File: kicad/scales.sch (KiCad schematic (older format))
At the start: 14 parts, among them J1 Serial, SW1 SW_DIP_x01, SW2 SW_DIP_x01, U1 AP2112

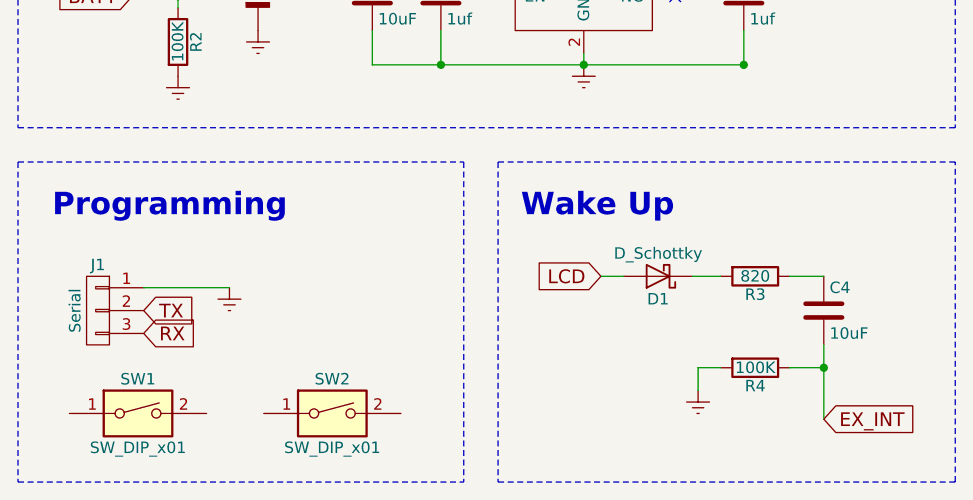
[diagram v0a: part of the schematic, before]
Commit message: Wake up is simply rising edge
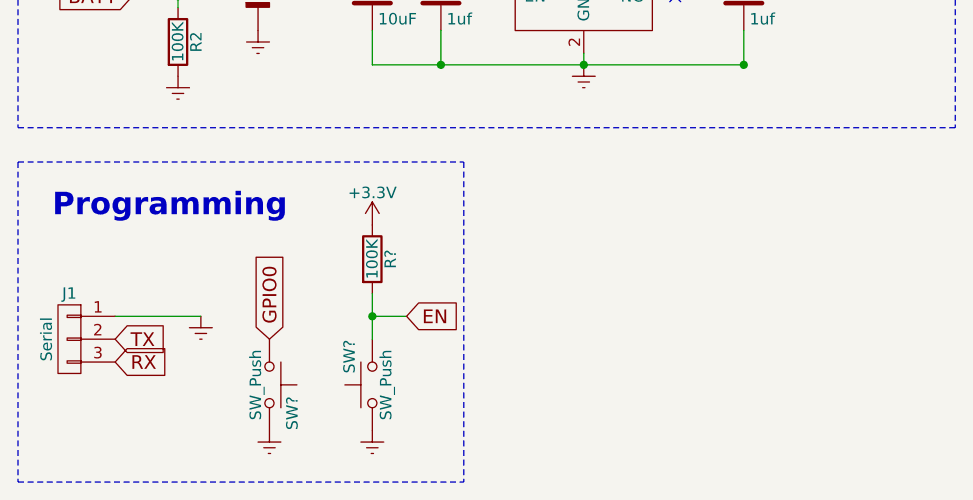
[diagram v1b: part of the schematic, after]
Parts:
- removed C4: 10uF, Capacitors_SMD:C_0805_HandSoldering, symbol C
- removed D1: D_Schottky, symbol D_Schottky
- removed R3: 820, Resistors_SMD:R_0805_HandSoldering, symbol R
- removed R4: 100K, Resistors_SMD:R_0805_HandSoldering, symbol R
- removed SW1, SW2: SW_DIP_x01, symbol SW_DIP_x01
- added R?: 100K, Resistors_SMD:R_0805_HandSoldering, symbol R
- added SW? (x2): SW_Push, symbol SW_Push
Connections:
- net +3V3: now also R?.1
- net Earth: now also SW?.1, SW?.2
- new net EN: R?.2, SW?.2
- new net GPIO0: SW?.1
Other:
- note removed: "Wake Up"
- moved on the sheet: J1
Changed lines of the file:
@@
 L Earth #PWR5
 U 1 1 59D62590
-P 1900 2825
-F 0 "#PWR5" H 1900 2575 50  0001 C CNN
-F 1 "Earth" H 1900 2675 50  0001 C CNN
-F 2 "" H 1900 2825 50  0000 C CNN
-F 3 "" H 1900 2825 50  0000 C CNN
-	1    1900 2825
-	-1   0    0    -1
-$EndComp
-$Comp
-L R R3
-U 1 1 59D62599
-P 4200 2775
-F 0 "R3" V 4280 2775 50  0000 C CNN
-F 1 "820" V 4200 2775 50  0000 C CNN
-F 2 "Resistors_SMD:R_0805_HandSoldering" V 4130 2775 50  0001 C CNN
-F 3 "" H 4200 2775 50  0000 C CNN
-	1    4200 2775
-	0    1    1    0
-$EndComp
-$Comp
-L Earth #PWR6
-U 1 1 59D6259A
-P 3950 3275
-F 0 "#PWR6" H 3950 3025 50  0001 C CNN
-F 1 "Earth" H 3950 3125 50  0001 C CNN
-F 2 "" H 3950 3275 50  0000 C CNN
-F 3 "" H 3950 3275 50  0000 C CNN
-	1    3950 3275
+P 1775 2950
+F 0 "#PWR5" H 1775 2700 50  0001 C CNN
+F 1 "Earth" H 1775 2800 50  0001 C CNN
+F 2 "" H 1775 2950 50  0000 C CNN
+F 3 "" H 1775 2950 50  0000 C CNN
+	1    1775 2950
 	-1   0    0    -1
 $EndComp
@@
 	1    0    0    -1
 $EndComp
-Text Notes 3175 2525 0    98   ~ 20
-Wake Up
 $Comp
 L Battery BT1
@@
 	1    0    0    -1
 $EndComp
-Text GLabel 1525 2925 2    60   Input ~ 0
+Text GLabel 1400 3050 2    60   Input ~ 0
 TX
-Text GLabel 1525 3025 2    60   Input ~ 0
+Text GLabel 1400 3150 2    60   Input ~ 0
 RX
 Text GLabel 1475 1550 0    60   Input ~ 0
@@
 Wire Wire Line
 	2825 1200 2825 1400
-Wire Notes Line
-	3075 2275 3075 3675
-Wire Notes Line
-	3075 3675 5075 3675
-Wire Notes Line
-	5075 3675 5075 2275
-Wire Notes Line
-	5075 2275 3075 2275
 Wire Notes Line
 	975  725  975  2125
@@
 	5075 725  5075 2125
 $Comp
-L C C4
-U 1 1 59D6390C
-P 4500 2925
-F 0 "C4" H 4525 3025 50  0000 L CNN
-F 1 "10uF" H 4525 2825 50  0000 L CNN
-F 2 "Capacitors_SMD:C_0805_HandSoldering" H 4538 2775 50  0001 C CNN
-F 3 "" H 4500 2925 50  0000 C CNN
-	1    4500 2925
-	1    0    0    -1
-$EndComp
-Text GLabel 3525 2775 0    60   Input ~ 0
-LCD
-$Comp
-L D_Schottky D1
-U 1 1 59D63AE4
-P 3775 2775
-F 0 "D1" H 3775 2875 50  0000 C CNN
-F 1 "D_Schottky" H 3775 2675 50  0000 C CNN
-F 2 "" H 3775 2775 50  0001 C CNN
-F 3 "" H 3775 2775 50  0001 C CNN
-	1    3775 2775
-	-1   0    0    1
-$EndComp
-Text GLabel 4500 3400 2    60   Input ~ 0
-EX_INT
-$Comp
-L R R4
-U 1 1 59D63D1D
-P 4200 3175
-F 0 "R4" V 4280 3175 50  0000 C CNN
-F 1 "100K" V 4200 3175 50  0000 C CNN
-F 2 "Resistors_SMD:R_0805_HandSoldering" V 4130 3175 50  0001 C CNN
-F 3 "" H 4200 3175 50  0000 C CNN
-	1    4200 3175
-	0    1    1    0
-$EndComp
-Wire Wire Line
-	3925 2775 4050 2775
-Wire Wire Line
-	3525 2775 3625 2775
-Wire Wire Line
-	4500 3075 4500 3400
-Wire Wire Line
-	4050 3175 3950 3175
-Wire Wire Line
-	3950 3175 3950 3275
-Wire Wire Line
-	4500 2775 4350 2775
-Wire Wire Line
-	4350 3175 4500 3175
-Connection ~ 4500 3175
-$Comp
 L CONN_01X03 J1
 U 1 1 59D64697
-P 1325 2925
-F 0 "J1" H 1325 3125 50  0000 C CNN
-F 1 "Serial" V 1425 2925 50  0000 C CNN
-F 2 "" H 1325 2925 50  0001 C CNN
-F 3 "" H 1325 2925 50  0001 C CNN
-	1    1325 2925
-	-1   0    0    -1
-$EndComp
-Wire Wire Line
-	1525 2825 1900 2825
-$Comp
-L SW_DIP_x01 SW1
-U 1 1 59D62C52
-P 1500 3375
-F 0 "SW1" H 1500 3525 50  0000 C CNN
-F 1 "SW_DIP_x01" H 1500 3225 50  0000 C CNN
-F 2 "" H 1500 3375 50  0001 C CNN
-F 3 "" H 1500 3375 50  0001 C CNN
-	1    1500 3375
-	1    0    0    -1
-$EndComp
-$Comp
-L SW_DIP_x01 SW2
-U 1 1 59D62D60
-P 2350 3375
-F 0 "SW2" H 2350 3525 50  0000 C CNN
-F 1 "SW_DIP_x01" H 2350 3225 50  0000 C CNN
-F 2 "" H 2350 3375 50  0001 C CNN
-F 3 "" H 2350 3375 50  0001 C CNN
-	1    2350 3375
-	1    0    0    -1
-$EndComp
+P 1200 3050
+F 0 "J1" H 1200 3250 50  0000 C CNN
+F 1 "Serial" V 1300 3050 50  0000 C CNN
+F 2 "" H 1200 3050 50  0001 C CNN
+F 3 "" H 1200 3050 50  0001 C CNN
+	1    1200 3050
+	-1   0    0    -1
+$EndComp
+Wire Wire Line
+	1400 2950 1775 2950
+$Comp
+L SW_Push SW?
+U 1 1 59D68B06
+P 2075 3250
+F 0 "SW?" H 2125 3350 50  0000 L CNN
+F 1 "SW_Push" H 2075 3190 50  0000 C CNN
+F 2 "" H 2075 3450 50  0001 C CNN
+F 3 "" H 2075 3450 50  0001 C CNN
+	1    2075 3250
+	0    1    1    0
+$EndComp
+$Comp
+L SW_Push SW?
+U 1 1 59D68B53
+P 2525 3250
+F 0 "SW?" H 2575 3350 50  0000 L CNN
+F 1 "SW_Push" H 2525 3190 50  0000 C CNN
+F 2 "" H 2525 3450 50  0001 C CNN
+F 3 "" H 2525 3450 50  0001 C CNN
+	1    2525 3250
+	0    -1   -1   0
+$EndComp
+Text GLabel 2075 3050 1    60   Input ~ 0
+GPIO0
+$Comp
+L Earth #PWR?
+U 1 1 59D68C6B
+P 2075 3450
+F 0 "#PWR?" H 2075 3200 50  0001 C CNN
+F 1 "Earth" H 2075 3300 50  0001 C CNN
+F 2 "" H 2075 3450 50  0000 C CNN
+F 3 "" H 2075 3450 50  0000 C CNN
+	1    2075 3450
+	-1   0    0    -1
+$EndComp
+Text GLabel 2675 2950 2    60   Input ~ 0
+EN
+$Comp
+L Earth #PWR?
+U 1 1 59D68D23
+P 2525 3450
+F 0 "#PWR?" H 2525 3200 50  0001 C CNN
+F 1 "Earth" H 2525 3300 50  0001 C CNN
+F 2 "" H 2525 3450 50  0000 C CNN
+F 3 "" H 2525 3450 50  0000 C CNN
+	1    2525 3450
+	-1   0    0    -1
+$EndComp
+$Comp
+L +3.3V #PWR?
+U 1 1 59D68DA9
+P 2525 2550
+F 0 "#PWR?" H 2525 2400 50  0001 C CNN
+F 1 "+3.3V" H 2525 2690 50  0000 C CNN
+F 2 "" H 2525 2550 50  0001 C CNN
+F 3 "" H 2525 2550 50  0001 C CNN
+	1    2525 2550
+	1    0    0    -1
+$EndComp
+$Comp
+L R R?
+U 1 1 59D68E04
+P 2525 2700
+F 0 "R?" V 2605 2700 50  0000 C CNN
+F 1 "100K" V 2525 2700 50  0000 C CNN
+F 2 "Resistors_SMD:R_0805_HandSoldering" V 2455 2700 50  0001 C CNN
+F 3 "" H 2525 2700 50  0001 C CNN
+	1    2525 2700
+	1    0    0    -1
+$EndComp
+Wire Wire Line
+	2525 2850 2525 3050
+Wire Wire Line
+	2675 2950 2525 2950
+Connection ~ 2525 2950
 $EndSCHEMATC

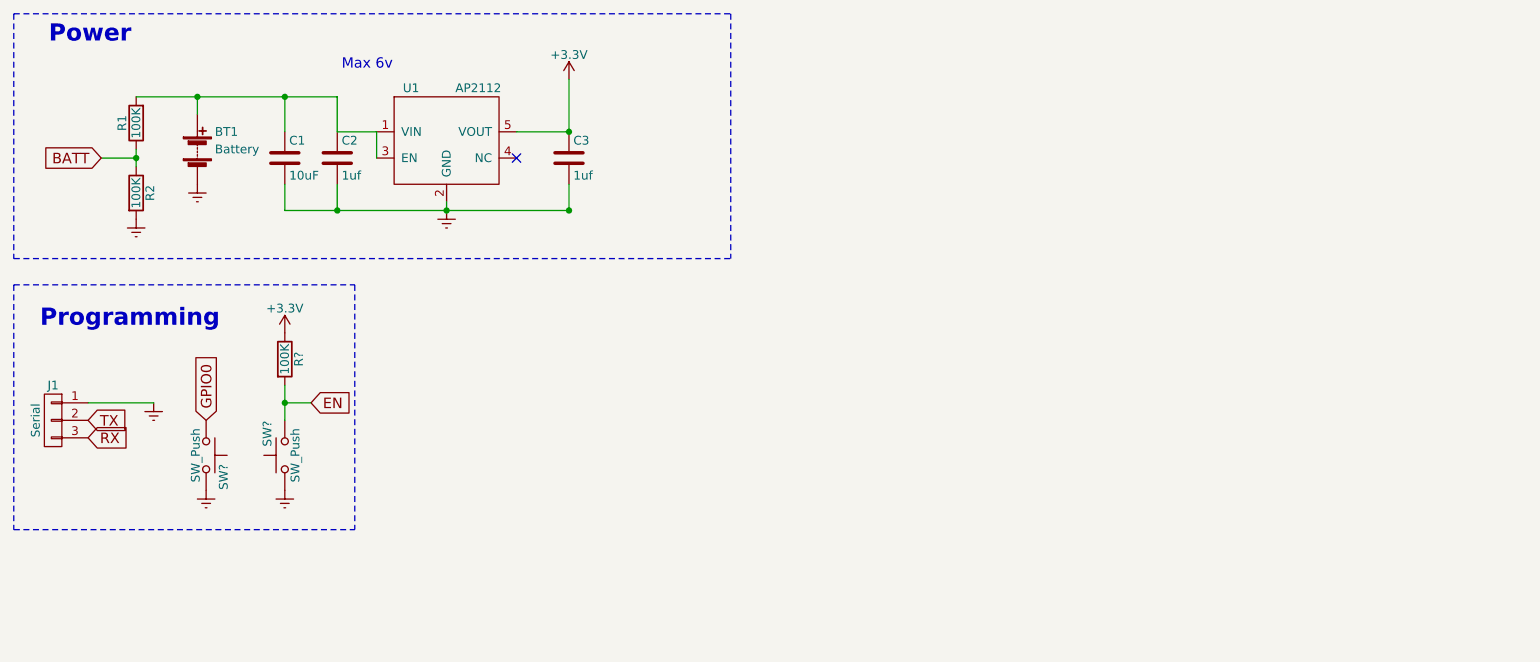
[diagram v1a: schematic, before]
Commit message: ESP32 WROOM
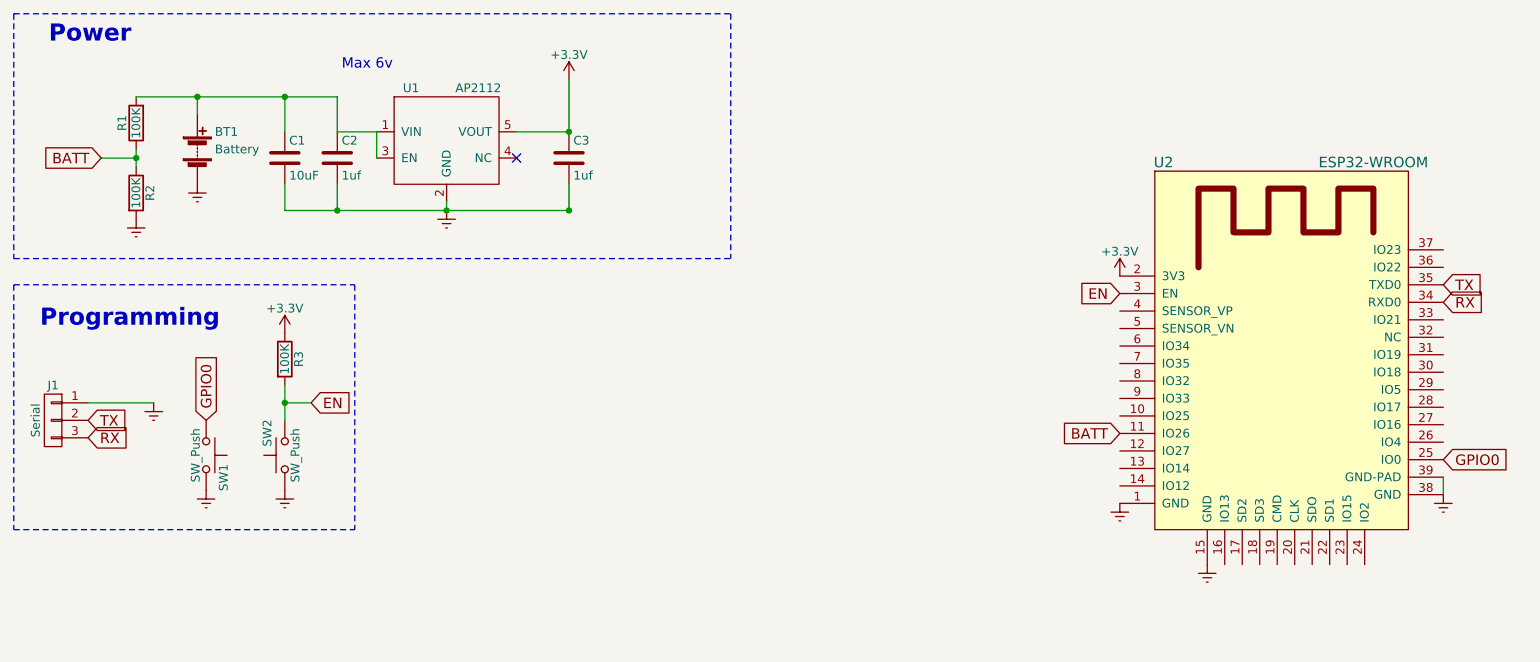
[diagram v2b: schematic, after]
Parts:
- added U2: ESP32-WROOM, ESP32-footprints-Lib:ESP32-WROOM, symbol ESP32-WROOM
- gave numbers to parts that had none: 3
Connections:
- net +3V3: now also U2.2 (3V3)
- net BATT: now also U2.11 (IO26)
- net EN: now also U2.3 (EN)
- net Earth: now also U2.1 (GND), U2.15 (GND), U2.38 (GND), U2.39 (GND-PAD)
- net GPIO0: now also U2.25 (IO0)
- net RX: now also U2.34 (RXD0)
- net TX: now also U2.35 (TXD0)
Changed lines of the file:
@@
 LIBS:valves
 LIBS:switches
+LIBS:ESP32-footprints-Shem-Lib
 LIBS:scales-cache
 EELAYER 25 0
@@
 $EndDescr
 $Comp
-L Earth #PWR5
+L Earth #PWR7
 U 1 1 59D62590
 P 1775 2950
-F 0 "#PWR5" H 1775 2700 50  0001 C CNN
+F 0 "#PWR7" H 1775 2700 50  0001 C CNN
 F 1 "Earth" H 1775 2800 50  0001 C CNN
 F 2 "" H 1775 2950 50  0000 C CNN
@@
 	1400 2950 1775 2950
 $Comp
-L SW_Push SW?
+L SW_Push SW1
 U 1 1 59D68B06
 P 2075 3250
-F 0 "SW?" H 2125 3350 50  0000 L CNN
+F 0 "SW1" H 2125 3350 50  0000 L CNN
 F 1 "SW_Push" H 2075 3190 50  0000 C CNN
 F 2 "" H 2075 3450 50  0001 C CNN
@@
 $EndComp
 $Comp
-L SW_Push SW?
+L SW_Push SW2
 U 1 1 59D68B53
 P 2525 3250
-F 0 "SW?" H 2575 3350 50  0000 L CNN
+F 0 "SW2" H 2575 3350 50  0000 L CNN
 F 1 "SW_Push" H 2525 3190 50  0000 C CNN
 F 2 "" H 2525 3450 50  0001 C CNN
@@
 GPIO0
 $Comp
-L Earth #PWR?
+L Earth #PWR8
 U 1 1 59D68C6B
 P 2075 3450
-F 0 "#PWR?" H 2075 3200 50  0001 C CNN
+F 0 "#PWR8" H 2075 3200 50  0001 C CNN
 F 1 "Earth" H 2075 3300 50  0001 C CNN
 F 2 "" H 2075 3450 50  0000 C CNN
@@
 EN
 $Comp
-L Earth #PWR?
+L Earth #PWR9
 U 1 1 59D68D23
 P 2525 3450
-F 0 "#PWR?" H 2525 3200 50  0001 C CNN
+F 0 "#PWR9" H 2525 3200 50  0001 C CNN
 F 1 "Earth" H 2525 3300 50  0001 C CNN
 F 2 "" H 2525 3450 50  0000 C CNN
@@
 $EndComp
 $Comp
-L +3.3V #PWR?
+L +3.3V #PWR6
 U 1 1 59D68DA9
 P 2525 2550
-F 0 "#PWR?" H 2525 2400 50  0001 C CNN
+F 0 "#PWR6" H 2525 2400 50  0001 C CNN
 F 1 "+3.3V" H 2525 2690 50  0000 C CNN
 F 2 "" H 2525 2550 50  0001 C CNN
@@
 $EndComp
 $Comp
-L R R?
+L R R3
 U 1 1 59D68E04
 P 2525 2700
-F 0 "R?" V 2605 2700 50  0000 C CNN
+F 0 "R3" V 2605 2700 50  0000 C CNN
 F 1 "100K" V 2525 2700 50  0000 C CNN
 F 2 "Resistors_SMD:R_0805_HandSoldering" V 2455 2700 50  0001 C CNN
@@
 	2675 2950 2525 2950
 Connection ~ 2525 2950
+$Comp
+L ESP32-WROOM U2
+U 1 1 59D7564C
+P 8250 2825
+F 0 "U2" H 7550 4075 60  0000 C CNN
+F 1 "ESP32-WROOM" H 8750 4075 60  0000 C CNN
+F 2 "ESP32-footprints-Lib:ESP32-WROOM" H 8600 4175 60  0001 C CNN
+F 3 "" H 7800 3275 60  0001 C CNN
+	1    8250 2825
+	1    0    0    -1
+$EndComp
+$Comp
+L +3.3V #PWR5
+U 1 1 59D75853
+P 7300 2225
+F 0 "#PWR5" H 7300 2075 50  0001 C CNN
+F 1 "+3.3V" H 7300 2365 50  0000 C CNN
+F 2 "" H 7300 2225 50  0001 C CNN
+F 3 "" H 7300 2225 50  0001 C CNN
+	1    7300 2225
+	1    0    0    -1
+$EndComp
+Text GLabel 7300 2325 0    60   Input ~ 0
+EN
+Text GLabel 9150 3275 2    60   Input ~ 0
+GPIO0
+Text GLabel 9150 2275 2    60   Input ~ 0
+TX
+Text GLabel 9150 2375 2    60   Input ~ 0
+RX
+$Comp
+L Earth #PWR12
+U 1 1 59D75FA7
+P 7800 3875
+F 0 "#PWR12" H 7800 3625 50  0001 C CNN
+F 1 "Earth" H 7800 3725 50  0001 C CNN
+F 2 "" H 7800 3875 50  0000 C CNN
+F 3 "" H 7800 3875 50  0000 C CNN
+	1    7800 3875
+	-1   0    0    -1
+$EndComp
+$Comp
+L Earth #PWR11
+U 1 1 59D76006
+P 7300 3525
+F 0 "#PWR11" H 7300 3275 50  0001 C CNN
+F 1 "Earth" H 7300 3375 50  0001 C CNN
+F 2 "" H 7300 3525 50  0000 C CNN
+F 3 "" H 7300 3525 50  0000 C CNN
+	1    7300 3525
+	-1   0    0    -1
+$EndComp
+$Comp
+L Earth #PWR10
+U 1 1 59D76035
+P 9150 3475
+F 0 "#PWR10" H 9150 3225 50  0001 C CNN
+F 1 "Earth" H 9150 3325 50  0001 C CNN
+F 2 "" H 9150 3475 50  0000 C CNN
+F 3 "" H 9150 3475 50  0000 C CNN
+	1    9150 3475
+	-1   0    0    -1
+$EndComp
+Wire Wire Line
+	9150 3375 9150 3475
+Text GLabel 7300 3125 0    60   Input ~ 0
+BATT
 $EndSCHEMATC

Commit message: Schematic
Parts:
- added J2: HX711, symbol CONN_01X04
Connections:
- net Earth: now also J2.4 (P4)
- net WCLK: now reaches U2.20 (CLK)
- net WCLK: now also J2.3 (P3)
- net WDATA: now reaches U2.21 (SDO)
- net WDATA: now also J2.2 (P2)
- net WAKE: now reaches U2.7 (IO35)
- net WAKE: now also J2.1 (P1)
- no-connect marks 1 -> 26
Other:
- note added: "HX711"
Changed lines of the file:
@@
 $EndDescr
 $Comp
-L Earth #PWR7
+L Earth #PWR8
 U 1 1 59D62590
 P 1775 2950
-F 0 "#PWR7" H 1775 2700 50  0001 C CNN
+F 0 "#PWR8" H 1775 2700 50  0001 C CNN
 F 1 "Earth" H 1775 2800 50  0001 C CNN
 F 2 "" H 1775 2950 50  0000 C CNN
@@
 	3450 1850 3450 1800
 Wire Wire Line
-	2525 1850 4150 1850
+	2525 1850 2825 1850
+Wire Wire Line
+	2825 1850 3450 1850
+Wire Wire Line
+	3450 1850 4150 1850
 Wire Wire Line
 	2825 1850 2825 1700
@@
 	3050 1550 3050 1400
 Wire Wire Line
-	1675 1200 2825 1200
+	1675 1200 2025 1200
+Wire Wire Line
+	2025 1200 2525 1200
+Wire Wire Line
+	2525 1200 2825 1200
 Wire Wire Line
 	2825 1200 2825 1400
@@
 Connection ~ 4150 1400
 Wire Wire Line
-	1675 1500 1675 1600
+	1675 1500 1675 1550
+Wire Wire Line
+	1675 1550 1675 1600
 Wire Wire Line
 	1675 1550 1475 1550
@@
 GPIO0
 $Comp
-L Earth #PWR8
+L Earth #PWR9
 U 1 1 59D68C6B
 P 2075 3450
-F 0 "#PWR8" H 2075 3200 50  0001 C CNN
+F 0 "#PWR9" H 2075 3200 50  0001 C CNN
 F 1 "Earth" H 2075 3300 50  0001 C CNN
 F 2 "" H 2075 3450 50  0000 C CNN
@@
 EN
 $Comp
-L Earth #PWR9
+L Earth #PWR10
 U 1 1 59D68D23
 P 2525 3450
-F 0 "#PWR9" H 2525 3200 50  0001 C CNN
+F 0 "#PWR10" H 2525 3200 50  0001 C CNN
 F 1 "Earth" H 2525 3300 50  0001 C CNN
 F 2 "" H 2525 3450 50  0000 C CNN
@@
 $EndComp
 Wire Wire Line
-	2525 2850 2525 3050
+	2525 2850 2525 2950
+Wire Wire Line
+	2525 2950 2525 3050
 Wire Wire Line
 	2675 2950 2525 2950
@@
 RX
 $Comp
-L Earth #PWR12
+L Earth #PWR13
 U 1 1 59D75FA7
 P 7800 3875
-F 0 "#PWR12" H 7800 3625 50  0001 C CNN
+F 0 "#PWR13" H 7800 3625 50  0001 C CNN
 F 1 "Earth" H 7800 3725 50  0001 C CNN
 F 2 "" H 7800 3875 50  0000 C CNN
@@
 $EndComp
 $Comp
-L Earth #PWR11
+L Earth #PWR12
 U 1 1 59D76006
 P 7300 3525
-F 0 "#PWR11" H 7300 3275 50  0001 C CNN
+F 0 "#PWR12" H 7300 3275 50  0001 C CNN
 F 1 "Earth" H 7300 3375 50  0001 C CNN
 F 2 "" H 7300 3525 50  0000 C CNN
@@
 $EndComp
 $Comp
-L Earth #PWR10
+L Earth #PWR11
 U 1 1 59D76035
 P 9150 3475
-F 0 "#PWR10" H 9150 3225 50  0001 C CNN
+F 0 "#PWR11" H 9150 3225 50  0001 C CNN
 F 1 "Earth" H 9150 3325 50  0001 C CNN
 F 2 "" H 9150 3475 50  0000 C CNN
@@
 Text GLabel 7300 3125 0    60   Input ~ 0
 BATT
+Text GLabel 8300 3875 3    60   Input ~ 0
+WCLK
+Text GLabel 8400 3875 3    60   Input ~ 0
+WDATA
+Text GLabel 7300 2725 0    60   Input ~ 0
+WAKE
+NoConn ~ 7300 2425
+NoConn ~ 7300 2525
+NoConn ~ 7300 2625
+NoConn ~ 7300 2825
+NoConn ~ 7300 2925
+NoConn ~ 7300 3025
+NoConn ~ 7300 3225
+NoConn ~ 7300 3325
+NoConn ~ 7300 3425
+NoConn ~ 7900 3875
+NoConn ~ 8000 3875
+NoConn ~ 8100 3875
+NoConn ~ 8200 3875
+NoConn ~ 8500 3875
+NoConn ~ 8600 3875
+NoConn ~ 8700 3875
+NoConn ~ 9150 3175
+NoConn ~ 9150 3075
+NoConn ~ 9150 2975
+NoConn ~ 9150 2875
+NoConn ~ 9150 2775
+NoConn ~ 9150 2675
+NoConn ~ 9150 2575
+NoConn ~ 9150 2175
+NoConn ~ 9150 2075
+Text Notes 3150 2525 0    98   ~ 20
+HX711
+Text GLabel 3900 3050 2    60   Input ~ 0
+WDATA
+Text GLabel 3900 2950 2    60   Input ~ 0
+WCLK
+$Comp
+L Earth #PWR7
+U 1 1 59D780D3
+P 4425 2850
+F 0 "#PWR7" H 4425 2600 50  0001 C CNN
+F 1 "Earth" H 4425 2700 50  0001 C CNN
+F 2 "" H 4425 2850 50  0000 C CNN
+F 3 "" H 4425 2850 50  0000 C CNN
+	1    4425 2850
+	-1   0    0    -1
+$EndComp
+Wire Wire Line
+	3900 2850 4425 2850
+Wire Notes Line
+	3050 2275 3050 3675
+Wire Notes Line
+	3050 3675 5075 3675
+Wire Notes Line
+	5075 3675 5075 2275
+Wire Notes Line
+	5075 2275 3050 2275
+$Comp
+L CONN_01X04 J2
+U 1 1 59D78492
+P 3700 3000
+F 0 "J2" H 3700 3250 50  0000 C CNN
+F 1 "HX711" V 3800 3000 50  0000 C CNN
+F 2 "" H 3700 3000 50  0001 C CNN
+F 3 "" H 3700 3000 50  0001 C CNN
+	1    3700 3000
+	-1   0    0    1
+$EndComp
+Text GLabel 3900 3150 2    60   Input ~ 0
+WAKE
 $EndSCHEMATC
